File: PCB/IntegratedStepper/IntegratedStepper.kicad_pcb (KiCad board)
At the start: 4 copper layers, 57 x 42.5 mm, 76 parts, among them IC1 DRV8844PWPR, IC2 SN65HVD230DR, IC3 LMR38020FSQDDARQ1, J1 8P8C, J2 8P8C, J3 Screw_Terminal_01x02, J4 Screw_Terminal_01x02, J5 Conn_01x05_Socket, Q1 SS8050-G, Q2 SS8050-G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

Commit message: init PCB dev area
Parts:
- removed J1, J2: 8P8C, easyeda2kicad:RJ45-TH_KH-RJ45-58-8P8C
- added Audio1: PJ-327C-4A, easyeda2kicad:AUDIO-SMD_PJ-327C-4A, F.Cu at (143.2, 119.9)
- added Audio2: PJ-327C-4A, easyeda2kicad:AUDIO-SMD_PJ-327C-4A, F.Cu at (93.4, 107.8)
- added J6: XT30PW-F, Connector_AMASS:AMASS_XT30PW-F_1x02_P2.50mm_Horizontal, F.Cu at (135.1, 114.0)
- added J7: XT30PW-F, Connector_AMASS:AMASS_XT30PW-F_1x02_P2.50mm_Horizontal, F.Cu at (104.2, 122.2)
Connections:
- net /DRV8844/EN3 renamed /DRV8844/EN4
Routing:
- net VCC: track 40.0 -> 47.6 mm
- net GND: track 269.4 -> 261.9 mm

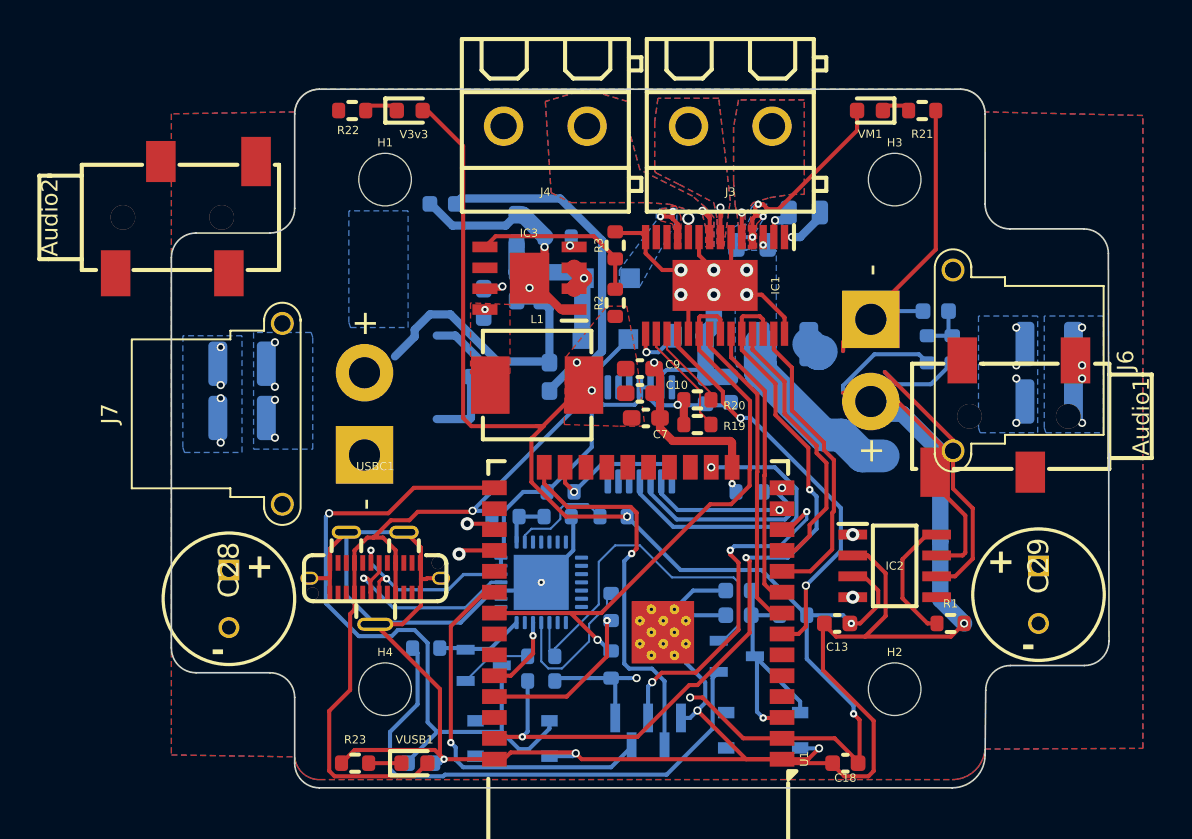
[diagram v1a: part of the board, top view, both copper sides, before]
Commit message: Update PCB with DRV8243 for 12A capacity
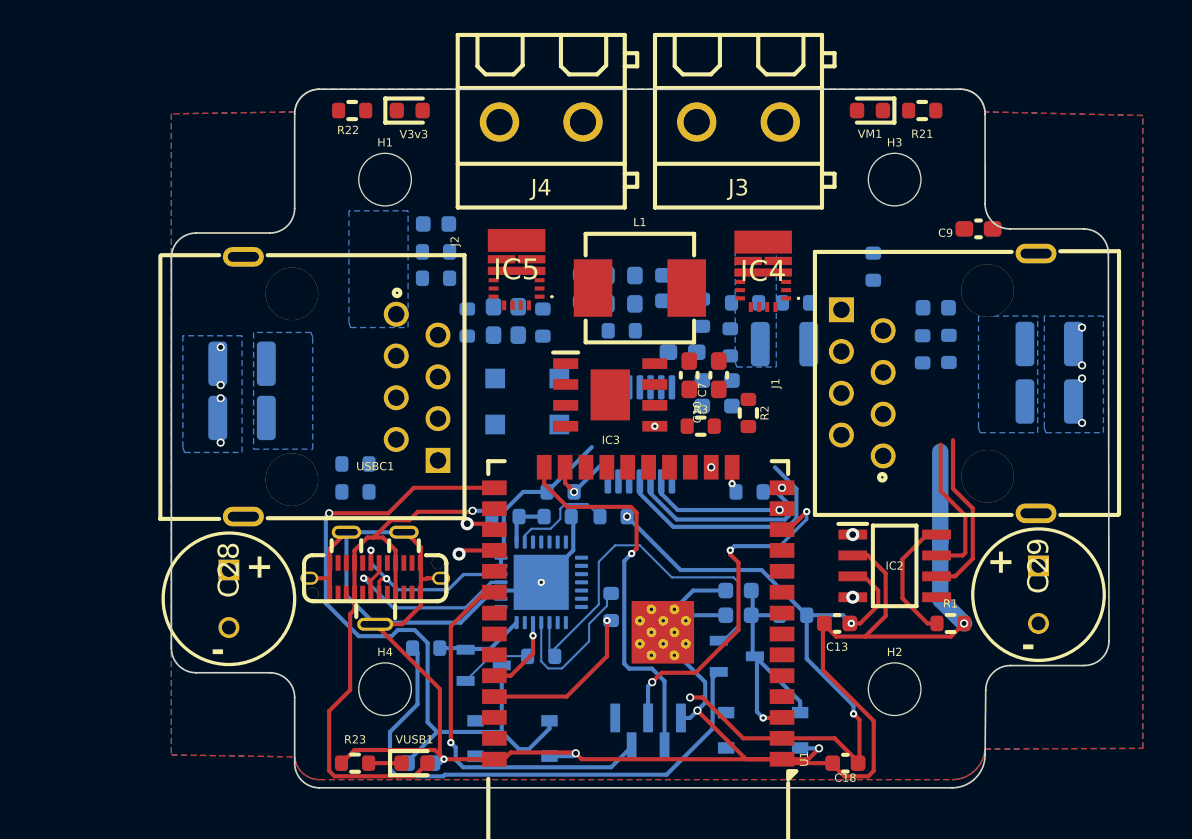
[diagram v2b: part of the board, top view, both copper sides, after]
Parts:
- removed Audio1, Audio2: PJ-327C-4A, easyeda2kicad:AUDIO-SMD_PJ-327C-4A
- removed C1, C3: 0.01uF, Capacitor_SMD:C_0805_2012Metric
- removed C2: 0.1uF, Capacitor_SMD:C_0805_2012Metric
- removed IC1: DRV8844PWPR, SamacSys_Parts:SOP65P640X120-29N
- removed J6, J7: XT30PW-F, Connector_AMASS:AMASS_XT30PW-F_1x02_P2.50mm_Horizontal
- removed R17, R18, R19, R20: 2k, Resistor_SMD:R_0603_1608Metric
- added IC4: DRV8243HQRXYRQ1, SamacSys_Parts:DRV8243HQRXYRQ1, F.Cu at (128.5, 111.1)
- added IC5: DRV8243HQRXYRQ1, SamacSys_Parts:DRV8243HQRXYRQ1, F.Cu at (113.5, 111.0)
- added J1: 8P8C, easyeda2kicad:RJ45-TH_KH-RJ45-58-8P8C, F.Cu at (139.2, 117.9)
- added J2: 8P8C, easyeda2kicad:RJ45-TH_KH-RJ45-58-8P8C, F.Cu at (102.8, 118.1)
- added R_DIAG1: 8.2k, Resistor_SMD:R_0603_1608Metric, B.Cu at (124.8, 113.6)
- added R_DIAG2: 8.2k, Resistor_SMD:R_0603_1608Metric, B.Cu at (110.5, 114.2)
- added R_DRV1: 2k, Resistor_SMD:R_0603_1608Metric, B.Cu at (108.6, 111.5)
- added R_IPROP1: 820, Resistor_SMD:R_0603_1608Metric, B.Cu at (135.2, 110.8)
- added R_IPROP2: 820, Resistor_SMD:R_0603_1608Metric, B.Cu at (117.4, 112.1)
- added R_MODE1: 8.2k, Resistor_SMD:R_0603_1608Metric, B.Cu at (130.5, 113.0)
- added R_MODE2: 8.2k, Resistor_SMD:R_0603_1608Metric, B.Cu at (115.1, 114.2)
- added R_SLEEP1: 2k, Resistor_SMD:R_0603_1608Metric, B.Cu at (126.5, 115.4)
- added R_SR1: 8.2k, Resistor_SMD:R_0603_1608Metric, B.Cu at (127.4, 113.0)
- added R_SR2: 8.2k, Resistor_SMD:R_0603_1608Metric, B.Cu at (108.6, 109.9)
- added R_nFAULT_1: 2k, Resistor_SMD:R_0603_1608Metric, B.Cu at (103.7, 124.5)
- added R_nFAULT_2: 2k, Resistor_SMD:R_0603_1608Metric, B.Cu at (103.7, 122.8)
- moved C9 22.3 mm to (141.6, 108.5), turned to 180 degrees
- moved C11 12.5 mm to (123.6, 116.0), turned to 180 degrees
- moved R3 12.2 mm to (124.7, 120.5), turned to 0 degrees
- moved C25 12.2 mm to (122.4, 112.1), turned to 90 degrees
- moved R2 10.5 mm to (127.6, 119.7), turned to -90 degrees
- moved IC3 8.63 mm to (119.2, 118.6), turned to 0 degrees
- moved L1 8.59 mm to (121.0, 112.1)
- moved D1 8.04 mm to (116.1, 119.0), turned to -90 degrees
- moved D2 7.70 mm to (112.2, 119.0), turned to -90 degrees
- moved C8 7.42 mm to (120.7, 112.2)
- moved R4 6.91 mm to (119.9, 114.7), turned to 0 degrees
- moved C6 6.63 mm to (119.0, 112.2)
- moved C7 5.14 mm to (125.8, 117.4), turned to -90 degrees
- moved C4 3.58 mm to (112.1, 114.1), turned to -90 degrees
- moved C10 3.20 mm to (124.0, 117.4), turned to -90 degrees
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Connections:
- net VCC renamed /3V3_VReg/VM
- J3 pad 1: /DRV8844/OUT1 -> /DRV8844/OUT2
- J3 pad 2: /DRV8844/OUT2 -> /DRV8844/OUT1
- J4 pad 1: /DRV8844/OUT3 -> /DRV8844/OUT4
- J4 pad 2: /DRV8844/OUT4 -> /DRV8844/OUT3
- U1 pad 26: unconnected-(U1-IO4-Pad26) -> /DRV8844/DRVOFF
- U1 pad 29: unconnected-(U1-IO5-Pad29) -> /DRV8844/NSLEEP
- U1 pad 31: /DRV8844/EN4 -> /DRV8844/NFAULT_1
- U1 pad 37: /DRV8844/EN1 -> /DRV8844/NFAULT_2
- U1 pad 6: unconnected-(U1-IO34-Pad6) -> IPROPI_1
- U1 pad 7: /DRV8844/NFAULT -> IPROPI_2
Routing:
- net GND: track 261.9 -> 162.7 mm, vias 24 -> 15
- net 3V3_VCC: track 141.2 -> 57.7 mm, vias 8 -> 4
- net /DRV8844/EN1: track 48.4 -> 0.00 mm, vias 3 -> 0
- net /3V3_VReg/VM: track 47.6 -> 6.13 mm, vias 13 -> 0
- net /DRV8844/EN4: track 35.9 -> 0.00 mm, vias 1 -> 0
- net /DRV8844/NFAULT: track 24.9 -> 0.00 mm, vias 2 -> 0
- net /DRV8844/IN4: track 19.2 -> 0.00 mm
- net /DRV8844/IN1: track 18.3 -> 0.00 mm
- net /DRV8844/IN3: track 17.4 -> 0.00 mm
- net /DRV8844/IN2: track 16.6 -> 0.00 mm
- net V_USB: track 48.7 -> 34.3 mm
- net CANL: track 48.4 -> 34.6 mm
- net VIN: track 11.5 -> 0.00 mm, vias 1 -> 0
- net CANH: track 52.8 -> 41.8 mm
- net Net-(IC3-FB): track 10.7 -> 0.00 mm, vias 0 -> 1
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- removed copper zone on F.Cu, net /3V3_VReg/VM
- removed copper zone on B.Cu, net /DRV8844/OUT1
- removed copper zone on F.Cu, net /DRV8844/OUT1
- removed copper zone on B.Cu, net /DRV8844/OUT2
- removed copper zone on F.Cu, net /DRV8844/OUT2
- removed copper zone on B.Cu, net /DRV8844/OUT3
- removed copper zone on F.Cu, net /DRV8844/OUT3
- removed copper zone on F.Cu, net 3V3_VCC
- removed copper zone on F.Cu, net Net-(IC3-SW)

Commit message: update layout temp
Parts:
- removed C22: 22uF, Capacitor_SMD:C_1210_3225Metric
- removed USBC1: TYPE-C 3.1_C168690, easyeda2kicad:USB-C-SMD_TYPE-C-USB-3
- added USB1: GT-USB-7038C, easyeda2kicad:USB-C-TH_G-SWITCH_GT-USB-7038X, F.Cu at (104.4, 129.4)
- moved D2 130.2 mm to (237.8, 84.5)
- moved D1 130.2 mm to (241.7, 84.5)
- moved C11 122.1 mm to (243.6, 93.3)
- moved C4 122.1 mm to (232.1, 91.5)
- moved C5 122.1 mm to (233.6, 91.5)
- moved C8 122.1 mm to (240.7, 89.5)
- moved C6 122.1 mm to (238.9, 89.5)
- moved R4 122.1 mm to (239.8, 92.0)
- moved IC3 118.4 mm to (235.7, 97.5)
- moved L1 116.6 mm to (235.7, 90.7)
- moved C7 110.4 mm to (235.4, 103.9)
- moved R3 110.4 mm to (234.3, 107.0)
- moved C10 110.4 mm to (233.6, 103.9)
- moved R2 110.4 mm to (237.2, 106.2)
- moved C9 76.7 mm to (215.9, 89.8)
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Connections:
- net V_USB renamed /3V3_VReg/V_USB
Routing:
- net GND: track 162.7 -> 0.00 mm, vias 15 -> 0
- net 3V3_VCC: track 57.7 -> 0.00 mm, vias 4 -> 0
- net IO0: track 44.4 -> 0.00 mm, vias 1 -> 0
- net CANH: track 41.8 -> 0.00 mm
- net CANL: track 34.6 -> 0.00 mm
- net /3V3_VReg/V_USB: track 34.3 -> 0.00 mm, vias 1 -> 0
- net Net-(Q1-B): track 32.8 -> 0.00 mm
- net /CAN_Transciever/CAN_RX: track 27.9 -> 0.00 mm, vias 2 -> 0
- net /CAN_Transciever/CAN_TX: track 25.6 -> 0.00 mm, vias 2 -> 0
- net /ESP32_MCU/ENC_IND: track 23.7 -> 0.00 mm, vias 1 -> 0
- net /ESP32_MCU/ENC-: track 23.2 -> 0.00 mm, vias 1 -> 0
- net RTS: track 23.1 -> 0.00 mm
- net /ESP32_MCU/ENC+: track 21.9 -> 0.00 mm, vias 3 -> 0
- net EN: track 15.4 -> 0.00 mm, vias 1 -> 0
- net /ESP32_MCU/M_MOSI: track 15.0 -> 0.00 mm, vias 1 -> 0
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
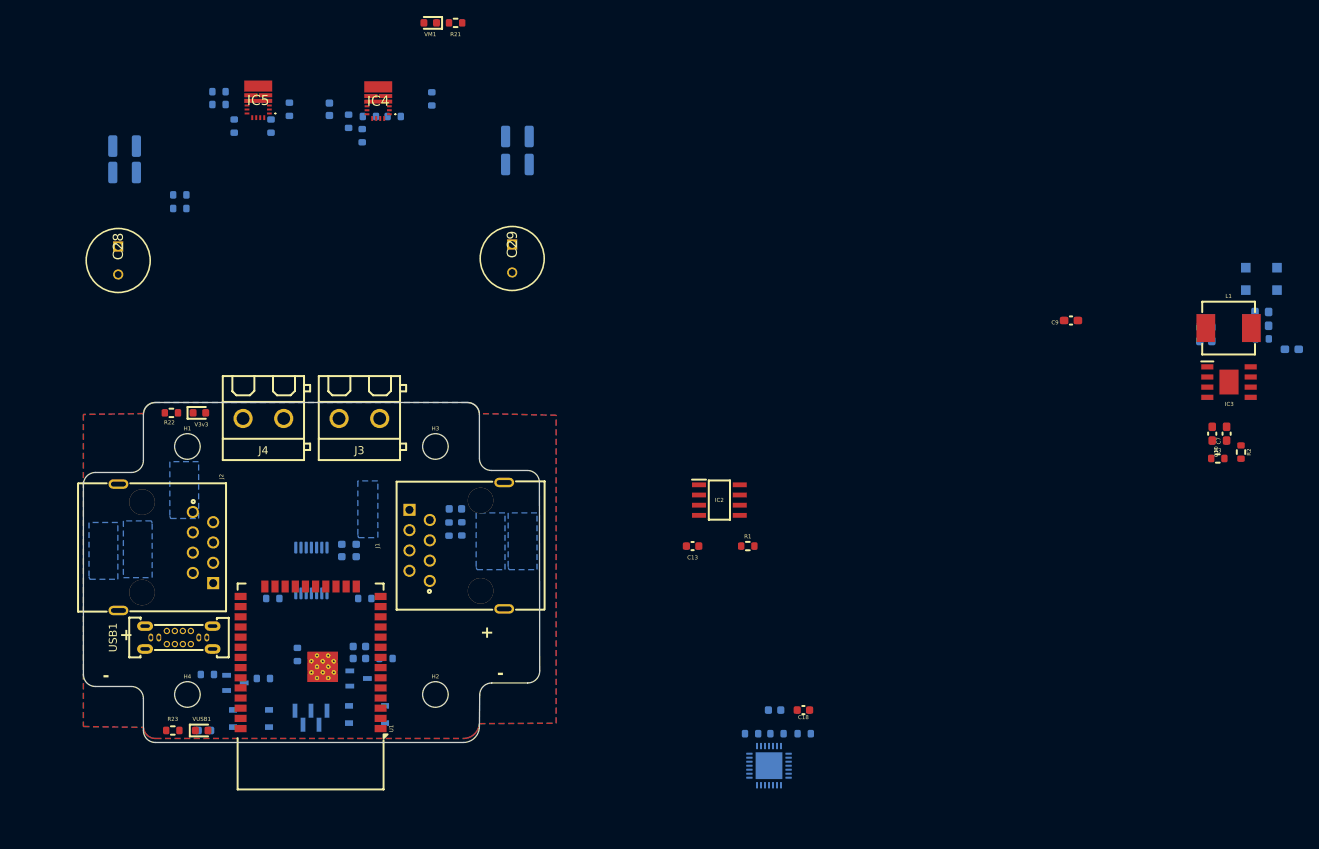
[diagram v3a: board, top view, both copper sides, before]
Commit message: update layout to XT30 + 3.5mm Jack
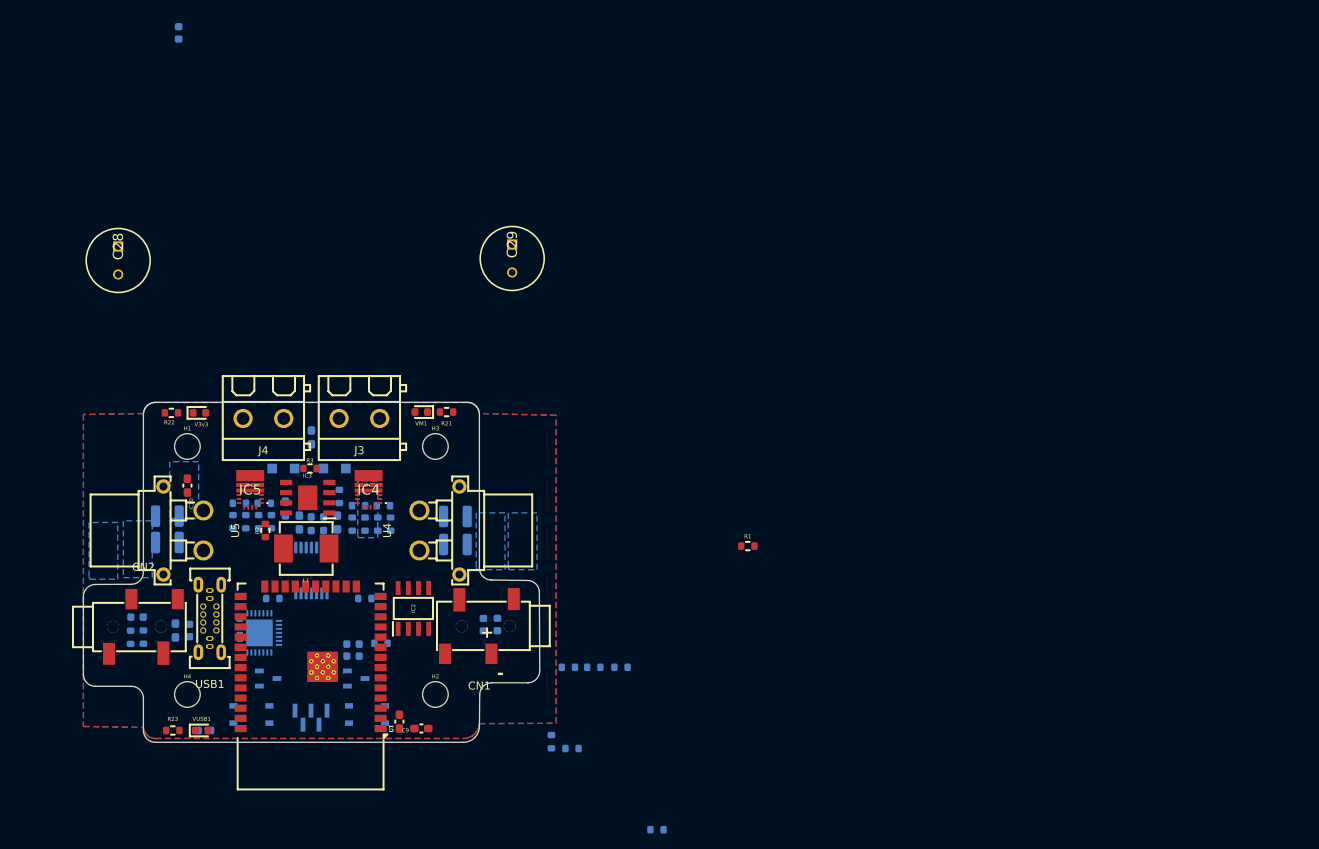
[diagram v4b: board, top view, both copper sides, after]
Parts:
- removed J1, J2: 8P8C, easyeda2kicad:RJ45-TH_KH-RJ45-58-8P8C
- added CN1: PJ-35825, easyeda2kicad:AUDIO-SMD_PJ-35825, F.Cu at (142.0, 128.0)
- added CN2: PJ-35825, easyeda2kicad:AUDIO-SMD_PJ-35825, F.Cu at (100.0, 128.0)
- added U4: XT30PW-F, easyeda2kicad:CONN-TH_XT30PW-F-1, F.Cu at (137.0, 116.0)
- added U5: XT30PW-F, easyeda2kicad:CONN-TH_XT30PW-F-1, F.Cu at (105.0, 116.0)
- C13, C18: moved to B.Cu
- moved C8 142.1 mm to (104.0, 128.5)
- moved C10 128.3 mm to (105.5, 110.4)
- moved C11 127.4 mm to (117.8, 113.2), turned to -90 degrees
- moved D2 122.6 mm to (117.5, 108.2), turned to 180 degrees
- moved R2 122.3 mm to (115.2, 116.0), turned to 90 degrees
- moved D1 120.2 mm to (123.9, 108.2), turned to 0 degrees
- moved C6 118.9 mm to (121.0, 104.4)
- moved L1 118.5 mm to (120.3, 118.2), turned to 180 degrees
- moved R4 117.0 mm to (124.5, 111.8), turned to -90 degrees
- moved IC3 116.1 mm to (120.5, 111.9), turned to 180 degrees
- moved C4 115.0 mm to (119.5, 115.0), turned to 90 degrees
- moved R3 113.5 mm to (120.8, 108.2)
- moved C5 111.8 mm to (124.2, 115.0), turned to 90 degrees
- moved C7 109.5 mm to (132.0, 139.9)
- moved C9 95.9 mm to (134.8, 140.8)
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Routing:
- added copper zone on In2.Cu, net /3V3_VReg/VM
- removed copper zone on In1.Cu, net /DRV8844/OUT4
- removed copper zone on In2.Cu, net /DRV8844/OUT4
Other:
- outline, holes or cut-outs redrawn

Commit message: update layout with pinout changes
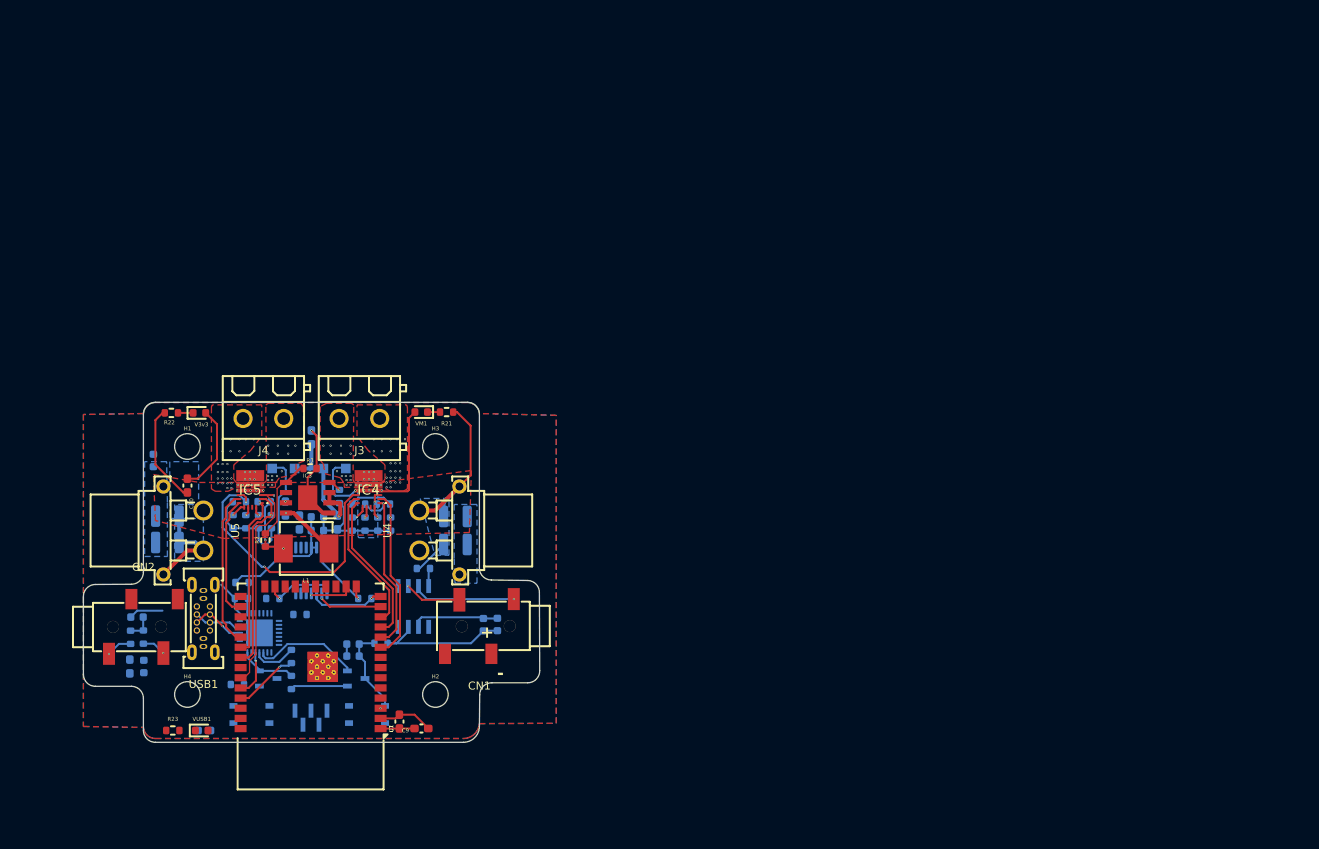
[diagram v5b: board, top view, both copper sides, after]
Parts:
- removed C28, C29: 100uF, SamacSys_Parts:CAPPRD350W65D800H1650
- IC2, R1: moved to B.Cu
- moved R14 55.5 mm to (111.8, 135.2), turned to 0 degrees
- moved C25 53.5 mm to (101.2, 107.2)
- moved R9 44.9 mm to (112.2, 124.5), turned to 180 degrees
- moved R10 42.2 mm to (112.3, 122.5)
- moved R12 40.7 mm to (119.6, 126.5)
- moved R1 40.6 mm to (135.0, 120.8), turned to 180 degrees
- moved R13 36.0 mm to (118.5, 135.0), turned to -90 degrees
- moved R11 34.2 mm to (118.5, 131.8)
- moved C19 7.26 mm to (100.0, 133.0)
- moved C8 7.26 mm to (98.3, 133.0)
- moved R2 1.20 mm to (115.2, 117.2)
- moved USB1 0.80 mm to (107.5, 127.0)
- moved IC2 0.25 mm to (133.8, 125.5)
- moved R_SLEEP1 0.20 mm to (130.0, 112.7)
- moved R_nFAULT_1 0.20 mm to (126.9, 112.7)
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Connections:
- net /DRV8844/IN2 renamed IN2
- IC4 pad 9: /DRV8844/IN1 -> IN1
- IC5 pad 10: /DRV8844/IN4 -> IN4
- IC5 pad 9: /DRV8844/IN3 -> IN3
- U1 pad 10: /DRV8844/IN1 -> /DRV8844/NFAULT_1
- U1 pad 12: /ESP32_MCU/ENC+ -> IN1
- U1 pad 24: /ESP32_MCU/ENC_IND -> /DRV8844/DRVOFF
- U1 pad 26: /DRV8844/DRVOFF -> IN4
- U1 pad 29: /DRV8844/NSLEEP -> IN3
- U1 pad 30: /ESP32_MCU/ENC- -> /DRV8844/NFAULT_2
- U1 pad 31: /DRV8844/NFAULT_1 -> IPROPI_2
- U1 pad 33: /ESP32_MCU/I2C_SDA -> /DRV8844/NSLEEP
- U1 pad 37: /DRV8844/NFAULT_2 -> unconnected-(U1-IO23-Pad37)
- U1 pad 6: IPROPI_1 -> unconnected-(U1-IO34-Pad6)
- U1 pad 7: IPROPI_2 -> /ESP32_MCU/ENC_IND
- U1 pad 8: /DRV8844/IN4 -> unconnected-(U1-IO32-Pad8)
- U1 pad 9: /DRV8844/IN3 -> IPROPI_1
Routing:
- net GND: track 0.00 -> 132.6 mm, vias 0 -> 14
- net 3V3_VCC: track 0.00 -> 59.1 mm, vias 0 -> 2
- net /DRV8844/NSLEEP: track 0.00 -> 43.3 mm, vias 0 -> 2
- net /DRV8844/DRVOFF: track 0.00 -> 35.7 mm, vias 0 -> 2
- net IPROPI_2: track 0.00 -> 23.8 mm, vias 0 -> 1
- net /DRV8844/NFAULT_1: track 0.00 -> 22.5 mm, vias 0 -> 1
- net IPROPI_1: track 0.00 -> 21.5 mm, vias 0 -> 1
- net /3V3_VReg/VM: track 0.00 -> 21.4 mm, vias 0 -> 10
- net /DRV8844/NFAULT_2: track 0.00 -> 20.9 mm, vias 0 -> 1
- net /3V3_VReg/V_USB: track 0.00 -> 19.9 mm
- net IN3: track 0.00 -> 19.7 mm
- net IN2: track 0.00 -> 19.1 mm
- net IN1: track 0.00 -> 18.3 mm
- net VIN: track 0.00 -> 17.6 mm, vias 0 -> 1
- net IN4: track 0.00 -> 16.1 mm
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- added copper zone on F.Cu, net /3V3_VReg/VM
- added copper zone on F.Cu, net /DRV8844/OUT3
- added copper zone on F.Cu, net /DRV8844/OUT4
